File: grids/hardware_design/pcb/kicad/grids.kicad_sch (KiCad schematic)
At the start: 107 parts, among them J17 AVR_SPI_PRG_6PTH, J2 PJ301WQP, Q1 20MHz, SW1 SW_MEC_5G_2LED

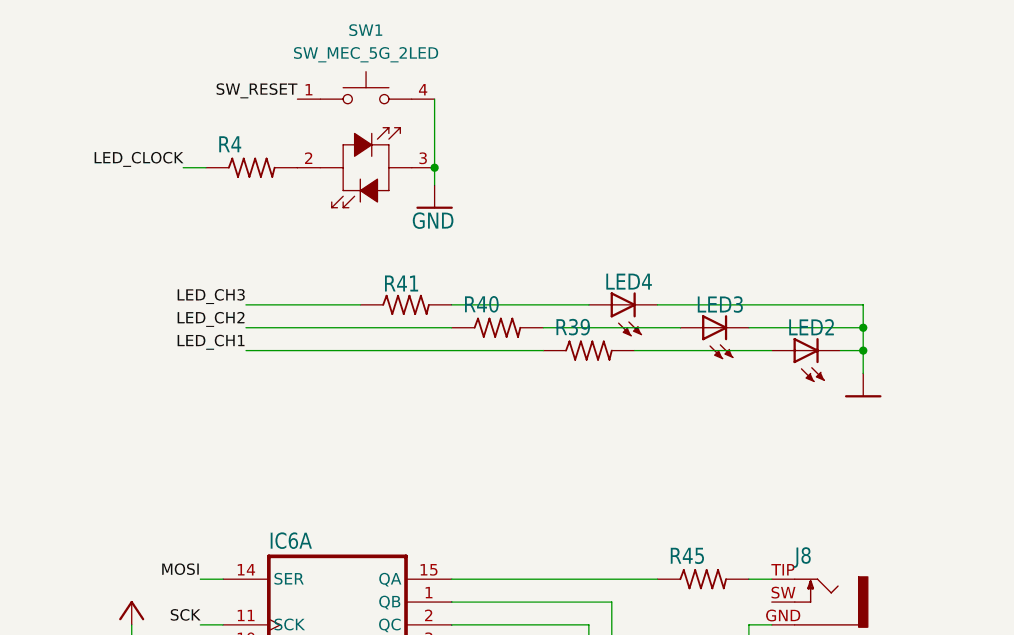
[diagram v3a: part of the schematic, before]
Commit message: add 0603 LEDs in parallel with other footprint
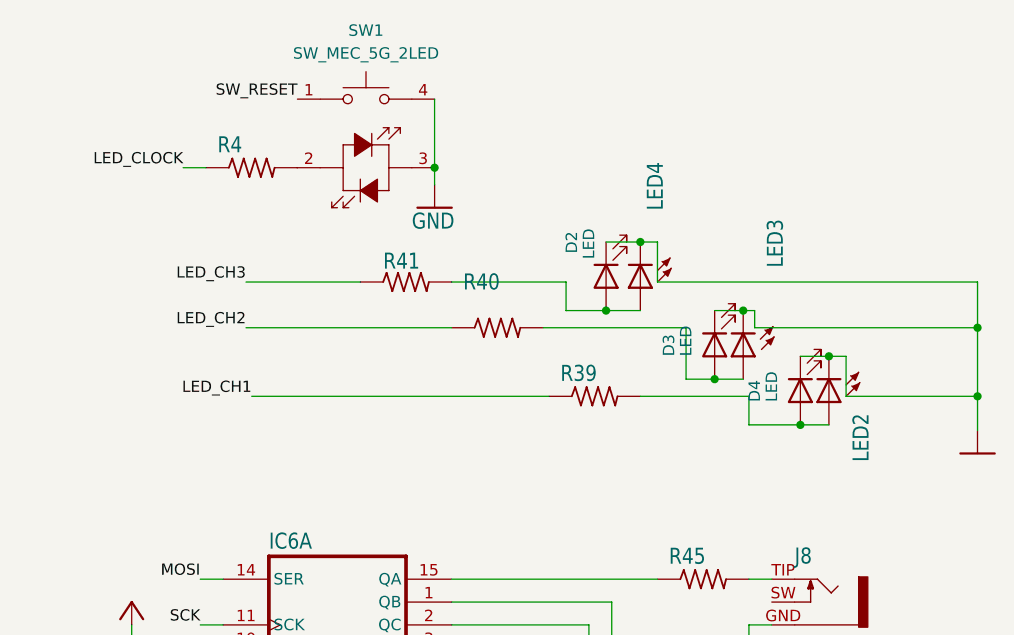
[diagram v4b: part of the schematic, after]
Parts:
- added D2, D3, D4: LED, LED_SMD:LED_0603_1608Metric, symbol Device:LED
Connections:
- net GND: now also D2.1 (K), D3.1 (K), D4.1 (K)
- net at LED4.A, R41.2: now also D2.2 (A)
- net at LED2.A, R39.2: now also D4.2 (A)
- net at LED3.A, R40.2: now also D3.2 (A)
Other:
- moved on the sheet: LED2, LED3, LED4, R39, R41
